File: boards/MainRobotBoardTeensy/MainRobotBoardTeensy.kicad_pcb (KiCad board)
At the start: 2 copper layers, 174 x 121.1 mm, 171 parts, among them J10 B4B-XH-A, J11 IDC, J13 B5B-XH-A, J14 B5B-XH-A, J2 B3B-XH-A, J3 B3B-XH-A, J4 B3B-XH-A, J5 B3B-XH-A, J6 B3B-XH-A, J7 B3B-XH-A, J8 B3B-XH-A, J9 B3B-XH-A, Q1 AO3400A, Q10 AO3400A, Q11 AO3400A, Q12 AO3400A, Q13 AO3400A, Q14 AO3400A, Q15 AO3400A, Q16 AO3400A, Q17 AO3400A, Q18 AO3400A, Q19 AO3400A, Q2 AO3400A, Q20 AO3400A, Q3 AO3400A, Q4 AO3400A, Q5 AO3400A, Q6 AO3400A, Q7 AO3400A, Q8 AO3400A, Q9 AO3400A, U1 Teensy4.0, U10 KWL-R1025BB, U11 SSD1306, U3 SN74HC08DR, U4 SN74HC08DR, U5 INA260, U6 SN74HC08DR, U7 ACS37220, U8 D0016A_N, U9 D0016A_N

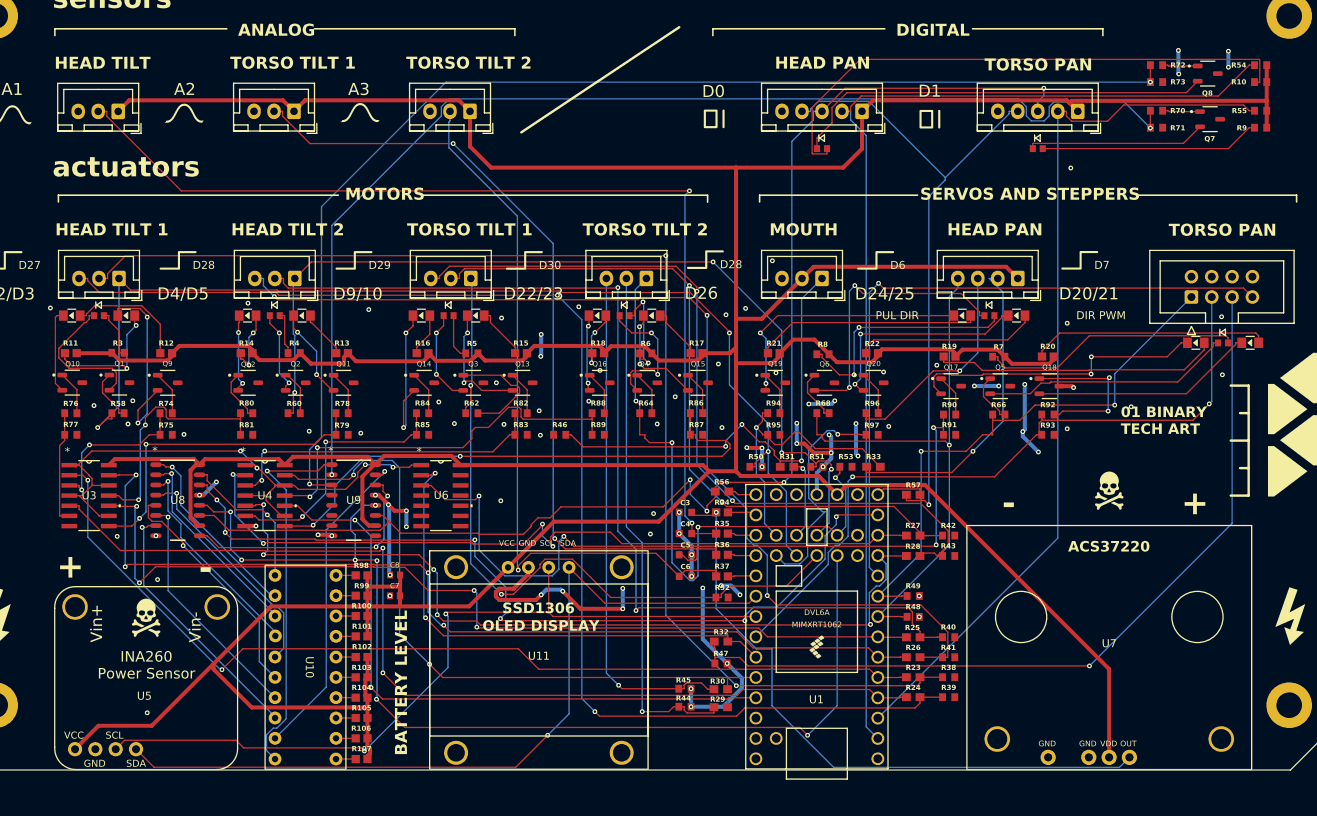
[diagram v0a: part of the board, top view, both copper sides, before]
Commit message: Add LED number displays to legs board and re-finalize
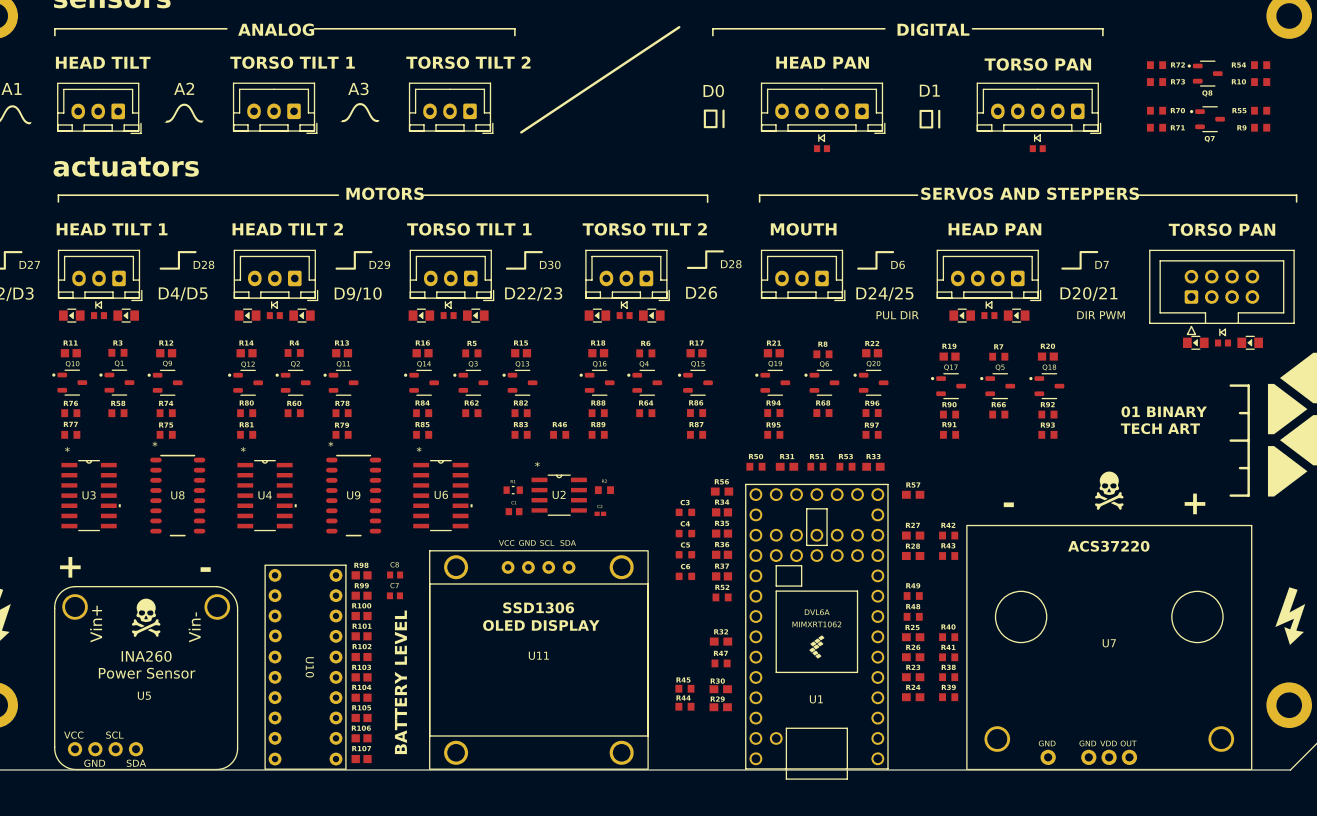
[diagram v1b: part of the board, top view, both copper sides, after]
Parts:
- added C1: 1uF, Capacitor1uF:CC0603JRX7R7BB105, F.Cu at (127.9, 125.5)
- added C2: 0.01uF, Capacitor0.01uF:C0402C103J4RACTU, F.Cu at (138.7, 125.7)
- added R1: 360K, Resistor360K:RC0603FR-07360KL, F.Cu at (127.8, 122.8)
- added R2: 10K, Resistor10K:CRCW060310K0FKEA, F.Cu at (139.2, 122.8)
- added U2: TLC555CDR, 555Timer:TLC555CDR, F.Cu at (133.6, 123.4)
- U8, U9: value D0016A_N -> SN74HC595DR
- moved U8 0.58 mm to (85.9, 123.4)
- moved U9 0.58 mm to (107.9, 123.4)
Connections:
- Q1 pad 2: Net-(D1-K) -> GND
- Q1 pad 3: GND -> Net-(D1-K)
- Q10 pad 2: Net-(D10-K) -> GND
- Q10 pad 3: GND -> Net-(D10-K)
- Q11 pad 2: Net-(D11-K) -> GND
- Q11 pad 3: GND -> Net-(D11-K)
- Q12 pad 2: Net-(D12-K) -> GND
- Q12 pad 3: GND -> Net-(D12-K)
- Q13 pad 2: Net-(D13-K) -> GND
- Q13 pad 3: GND -> Net-(D13-K)
- Q14 pad 2: Net-(D14-K) -> GND
- Q14 pad 3: GND -> Net-(D14-K)
- Q15 pad 2: Net-(D15-K) -> GND
- Q15 pad 3: GND -> Net-(D15-K)
- Q16 pad 2: Net-(D16-K) -> GND
- Q16 pad 3: GND -> Net-(D16-K)
- Q17 pad 2: Net-(D17-K) -> GND
- Q17 pad 3: GND -> Net-(D17-K)
- Q18 pad 2: Net-(D18-K) -> GND
- Q18 pad 3: GND -> Net-(D18-K)
- Q19 pad 2: Net-(D19-K) -> GND
- Q19 pad 3: GND -> Net-(D19-K)
- Q2 pad 2: Net-(D2-K) -> GND
- Q2 pad 3: GND -> Net-(D2-K)
- Q20 pad 2: Net-(D20-K) -> GND
- Q20 pad 3: GND -> Net-(D20-K)
- Q3 pad 2: Net-(D3-K) -> GND
- Q3 pad 3: GND -> Net-(D3-K)
- Q4 pad 2: Net-(D4-K) -> GND
- Q4 pad 3: GND -> Net-(D4-K)
- Q5 pad 2: Net-(D5-K) -> GND
- Q5 pad 3: GND -> Net-(D5-K)
- Q6 pad 2: Net-(D6-K) -> GND
- Q6 pad 3: GND -> Net-(D6-K)
- Q7 pad 2: Net-(D7-K) -> GND
- Q7 pad 3: GND -> Net-(D7-K)
- Q8 pad 2: Net-(D8-K) -> GND
- Q8 pad 3: GND -> Net-(D8-K)
- Q9 pad 2: Net-(D9-K) -> GND
- Q9 pad 3: GND -> Net-(D9-K)
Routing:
- net +3.3V: track 698.6 -> 0.00 mm
- net SCK: track 166.3 -> 0.00 mm, vias 4 -> 0
- net Net-(J5-Pin_3): track 159.9 -> 0.00 mm, vias 2 -> 0
- net Net-(J5-Pin_2): track 156.4 -> 0.00 mm, vias 2 -> 0
- net HEADENCODERST: track 150.3 -> 0.00 mm, vias 2 -> 0
- net TORSOENCODERST: track 147.7 -> 0.00 mm, vias 2 -> 0
- net HEADTILT1EN: track 136.6 -> 0.00 mm, vias 3 -> 0
- net CSHEAD: track 135.2 -> 0.00 mm
- net RCLK: track 134.1 -> 0.00 mm, vias 7 -> 0
- net GND: track 133.1 -> 0.00 mm, vias 94 -> 0
- net Net-(J6-Pin_3): track 128.7 -> 0.00 mm, vias 3 -> 0
- net Net-(J6-Pin_2): track 126.4 -> 0.00 mm, vias 2 -> 0
- net HEADTILT1LPWM: track 124.9 -> 0.00 mm, vias 2 -> 0
- net Net-(J2-Pin_2): track 124.9 -> 0.00 mm, vias 2 -> 0
- net HEADTILT1RPWM: track 121.4 -> 0.00 mm, vias 2 -> 0
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
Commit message: Re-finalize main robot board
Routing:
- net +3.3V: track 0.00 -> 681.5 mm
- net TORSOENCODERST: track 0.00 -> 176.8 mm, vias 0 -> 4
- net Net-(J5-Pin_3): track 0.00 -> 170.1 mm, vias 0 -> 5
- net SCK: track 0.00 -> 169.4 mm, vias 0 -> 5
- net HEADENCODERST: track 0.00 -> 168.8 mm, vias 0 -> 2
- net Net-(J5-Pin_2): track 0.00 -> 168.5 mm, vias 0 -> 4
- net Net-(D8-A): track 0.00 -> 163.2 mm
- net Net-(J7-Pin_2): track 0.00 -> 149.8 mm, vias 0 -> 3
- net HEADTILT1EN: track 0.00 -> 146.4 mm, vias 0 -> 5
- net Net-(J6-Pin_3): track 0.00 -> 145.8 mm, vias 0 -> 5
- net CSHEAD: track 0.00 -> 145.3 mm, vias 0 -> 1
- net HEADTILT1RPWM: track 0.00 -> 141.5 mm, vias 0 -> 5
- net HEADTILT1LPWM: track 0.00 -> 134.1 mm, vias 0 -> 3
- net SDA: track 0.00 -> 132.1 mm, vias 0 -> 1
- net Net-(J6-Pin_2): track 0.00 -> 130.8 mm, vias 0 -> 4
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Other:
- board text added: "01binary.us"
- board text removed: "01 BINARY TECH ART"

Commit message: Final board export after testing
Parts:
- C2: value 0.01uF -> 10nF
- R100, R101, R102, R103, R104, R105, R106, R107, R98, R99: value 150R -> 470R; footprint Resistor150:RESC1607X60N -> Resistor470:RC0603FR-07470RL
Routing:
- net TORSOTILT1LPWM: track 106.7 -> 96.3 mm
- net TORSOTILT2LPWM: track 77.7 -> 79.9 mm
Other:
- board text added: "3V3"
- board text added: "CS"
- board text added: "DIR"
- board text added: "EN"
- board text added: "ENA"
- board text added: "GND"
- board text added: "LED1"
- board text added: "LED10"
- board text added: "LED2"
- board text added: "LED3"
- board text added: "LED4"
- board text added: "LED5"
- board text added: "LED6"
- board text added: "LED7"
- board text added: "LED8"
- board text added: "LED9"
- board text added: "LPW"
- board text added: "MIS"
- board text added: "PUL"
- board text added: "PWM"
- board text added: "RPW"
- board text added: "SCK"
- board text added: "SIG"
- board text added: "STA"

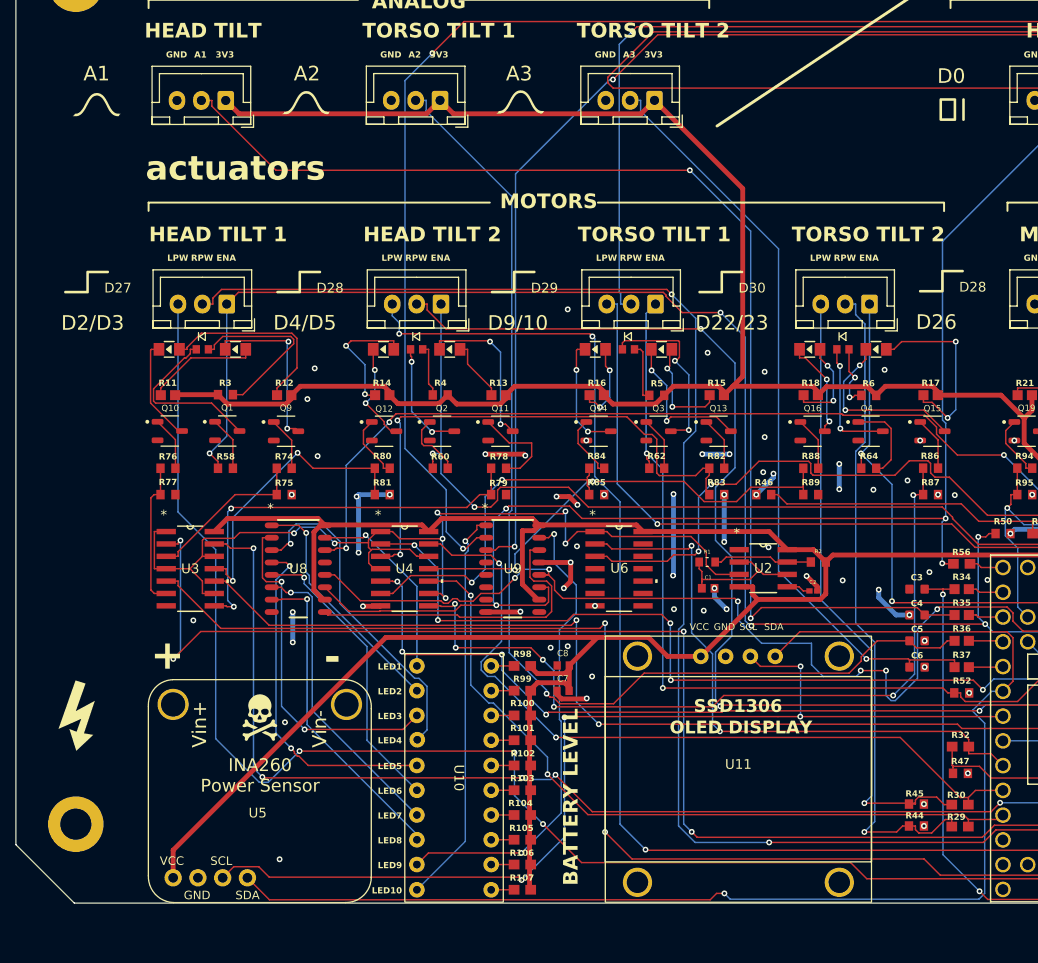
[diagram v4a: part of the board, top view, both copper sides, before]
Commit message: Leg board re-do LED displays, main board prepare for re-routing
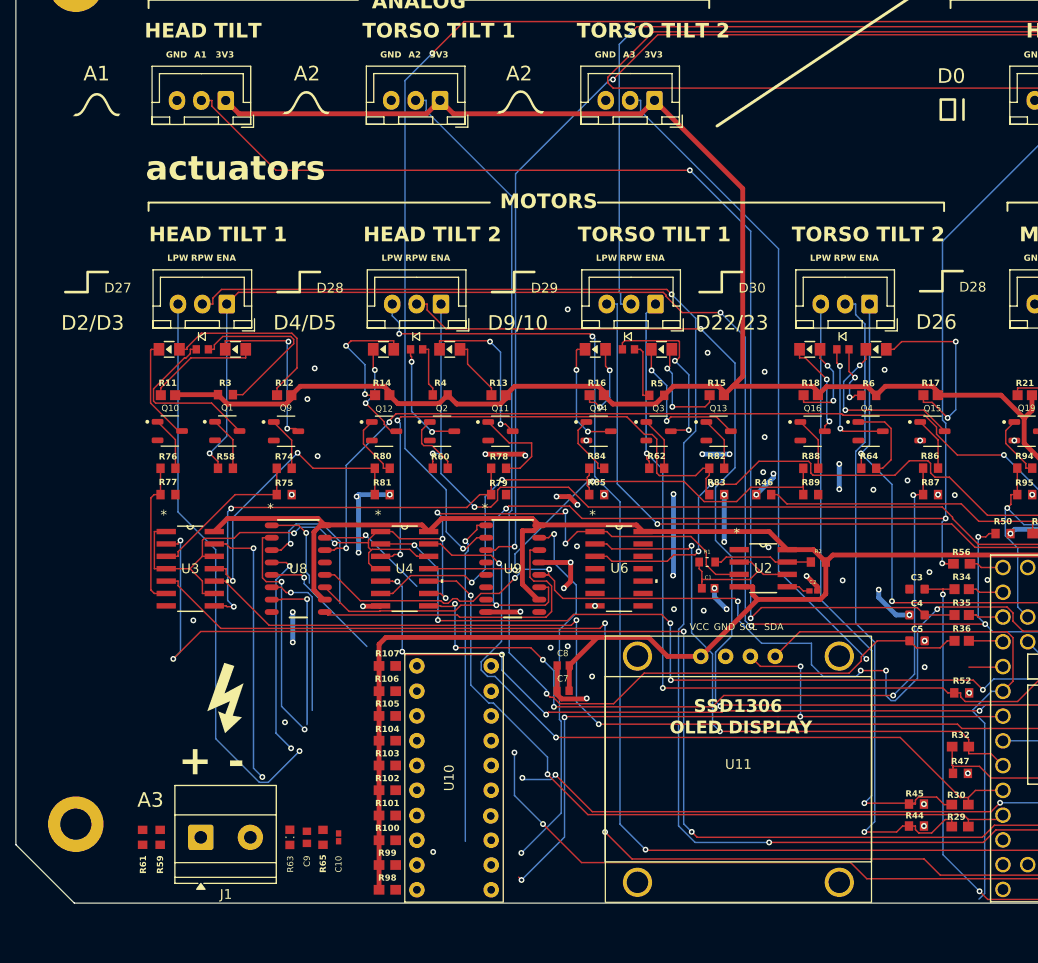
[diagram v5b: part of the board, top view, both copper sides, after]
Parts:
- removed C6: 47nF, Capacitor47nF:CAPC1608X90N
- removed R37: 2.2K, Resistor2.2K:RC0603FR-072K2L
- removed U5: INA260, INA260:INA260
- added C10: 10nF, Capacitor0.01uF:C0402C103J4RACTU, F.Cu at (90.0, 151.0)
- added C9: 100nF, Capacitor100nF:CC0603KRX7R9BB104, F.Cu at (86.8, 151.0)
- added J1: Screw_Terminal_01x02, TerminalBlock_Phoenix:TerminalBlock_Phoenix_MKDS-1,5-2-5.08_1x02_P5.08mm_Horizontal, F.Cu at (75.9, 151.0)
- added R59: 100K, Resistor100K:CRCW0603100KFKEA, F.Cu at (71.7, 151.0)
- added R61: 100K, Resistor100K:CRCW0603100KFKEA, F.Cu at (69.9, 151.0)
- added R63: 22K, Resistor22K:0603WAF2202T5E, F.Cu at (85.0, 151.0)
- added R65: 1K, Resistor1K:RCG06031K00FKEA, F.Cu at (88.4, 151.0)
- moved R107 26.8 mm to (95.0, 133.4), turned to 180 degrees
- moved R98 26.8 mm to (95.0, 156.4), turned to 180 degrees
- moved R99 22.6 mm to (95.0, 153.8), turned to 180 degrees
- moved R106 22.5 mm to (95.0, 136.0), turned to 180 degrees
- moved R100 18.9 mm to (95.0, 151.3), turned to 180 degrees
- moved R105 18.8 mm to (95.0, 138.6), turned to 180 degrees
- moved R101 15.9 mm to (95.0, 148.8), turned to 180 degrees
- moved R104 15.8 mm to (95.0, 141.1), turned to 180 degrees
- moved R102 14.1 mm to (95.0, 146.2), turned to 180 degrees
- moved R103 14.1 mm to (95.0, 143.6), turned to 180 degrees
- turned U10 to 90 degrees
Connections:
- C5 pad 1: Net-(J3-Pin_2) -> TORSO1
- J3 pad 2: Net-(J3-Pin_2) -> TORSO1
- J4 pad 2: Net-(J4-Pin_2) -> TORSO1
- R36 pad 1: Net-(J3-Pin_2) -> TORSO1
- R36 pad 2: TORSO1 -> Net-(U1-16_A2_RX4_SCL1)
- U1 pad 23: TORSO1 -> Net-(U1-16_A2_RX4_SCL1)
- U1 pad 24: TORSO2 -> VSENSE
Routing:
- net TORSO1: track 3.54 -> 181.3 mm, vias 0 -> 2
- net Net-(J3-Pin_2): track 113.3 -> 0.00 mm, vias 1 -> 0
- net Net-(J4-Pin_2): track 78.5 -> 0.00 mm, vias 1 -> 0
- net SDA: track 132.1 -> 55.6 mm, vias 1 -> 0
- net +3.3V: track 681.5 -> 644.4 mm
- net SCL: track 106.0 -> 74.7 mm
- net HEADTILT2LPWM: track 126.6 -> 100.1 mm
- net Net-(J5-Pin_3): track 170.1 -> 148.3 mm
- net LED4: track 34.6 -> 16.2 mm
- net LED6: track 30.0 -> 13.2 mm
- net LED8: track 33.0 -> 16.5 mm
- net LED2: track 24.7 -> 9.14 mm
- net LED7: track 31.4 -> 16.2 mm
- net LED5: track 35.6 -> 21.9 mm
- net LED3: track 35.4 -> 23.3 mm
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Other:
- board text removed: "BATTERY LEVEL"
- board text removed: "LED1"
- board text removed: "LED10"
- board text removed: "LED2"
- board text removed: "LED3"
- board text removed: "LED4"
- board text removed: "LED5"
- board text removed: "LED6"
- board text removed: "LED7"
- board text removed: "LED8"
- board text removed: "LED9"

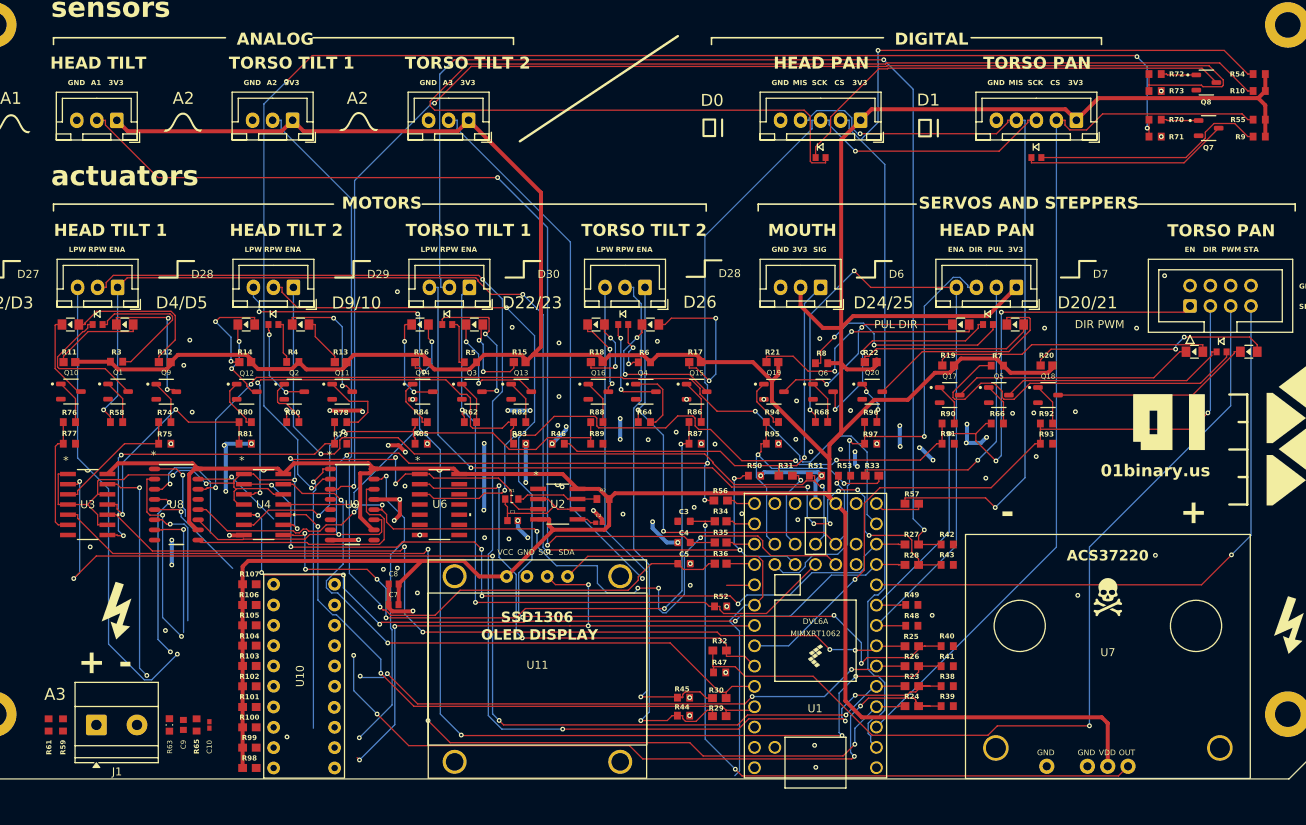
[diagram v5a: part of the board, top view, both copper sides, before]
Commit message: Re-route main board after flipping battery meter and removing INA260
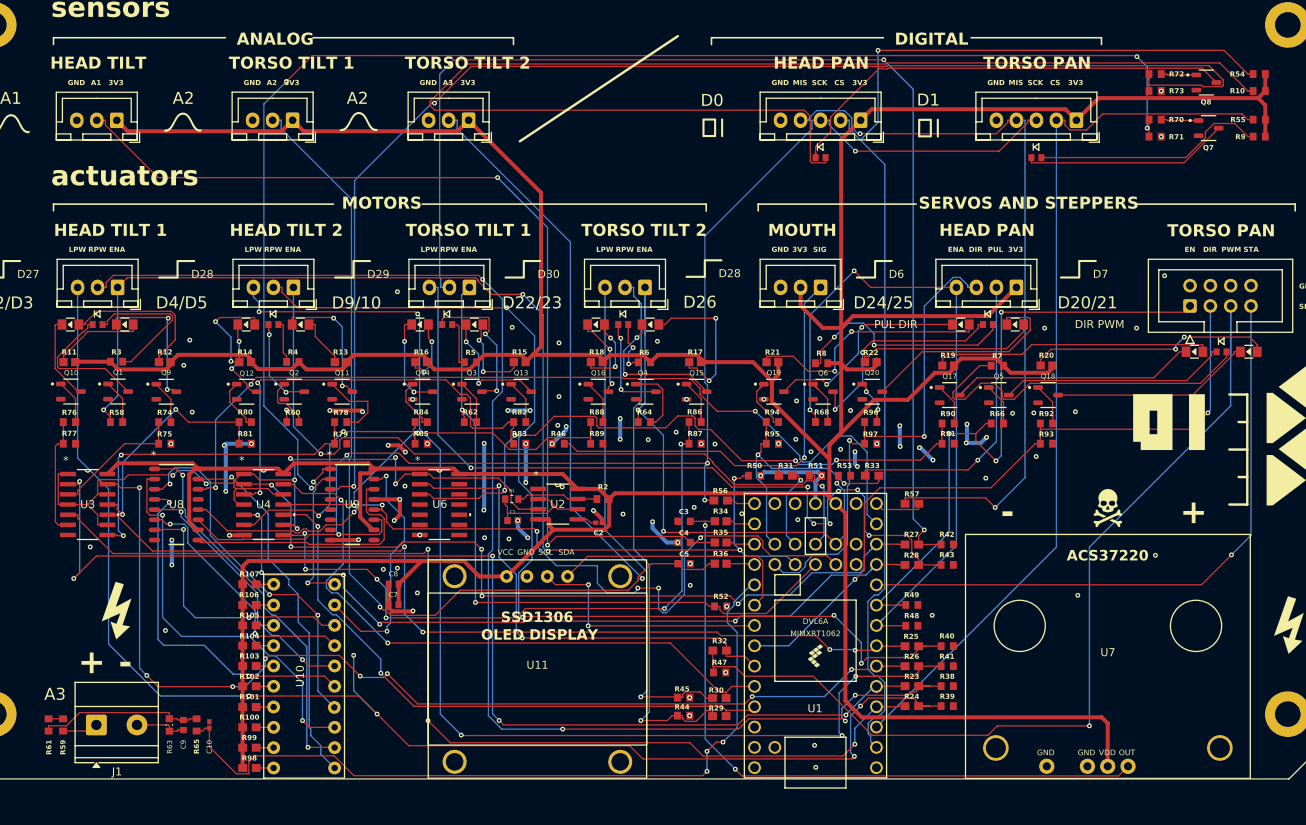
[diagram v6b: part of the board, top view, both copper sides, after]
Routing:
- net VSENSE: track 3.52 -> 98.3 mm, vias 0 -> 3
- net SCL: track 74.7 -> 32.3 mm, vias 4 -> 2
- net LED2: track 9.14 -> 47.9 mm, vias 1 -> 2
- net LED1: track 11.7 -> 46.0 mm
- net HEADTILT2LPWM: track 100.1 -> 130.8 mm, vias 6 -> 8
- net LED4: track 16.2 -> 46.5 mm, vias 1 -> 3
- net LED3: track 23.3 -> 49.9 mm
- net Net-(J5-Pin_3): track 148.3 -> 173.7 mm
- net SDA: track 55.6 -> 31.6 mm
- net LED5: track 21.9 -> 44.2 mm
- net Net-(C9-Pad2): track 0.00 -> 20.7 mm
- net LED6: track 13.2 -> 33.0 mm, vias 1 -> 2
- net LED8: track 16.5 -> 33.2 mm, vias 1 -> 2
- net LED7: track 16.2 -> 31.9 mm, vias 1 -> 2
- net LED10: track 34.1 -> 19.7 mm, vias 1 -> 2
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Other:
- board text removed: "01binary.us"
